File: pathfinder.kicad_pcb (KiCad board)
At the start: 2 copper layers, 59 x 46 mm, 12 parts, among them SW1 SW_Push, SW2 SW_Push, SW3 SW_Push, U1 XIAO-RP2040-DIP

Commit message: doing silkboard designs
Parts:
- moved D2 0.38 mm to (129.5, 112.2)
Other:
- board text added: "Keystorm X3"

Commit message: more silkscreen designs cuz why not
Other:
- board text added: "@hackclub"
- board text added: "made by: https://shashwat.cc"
- board text added: "oss hw"

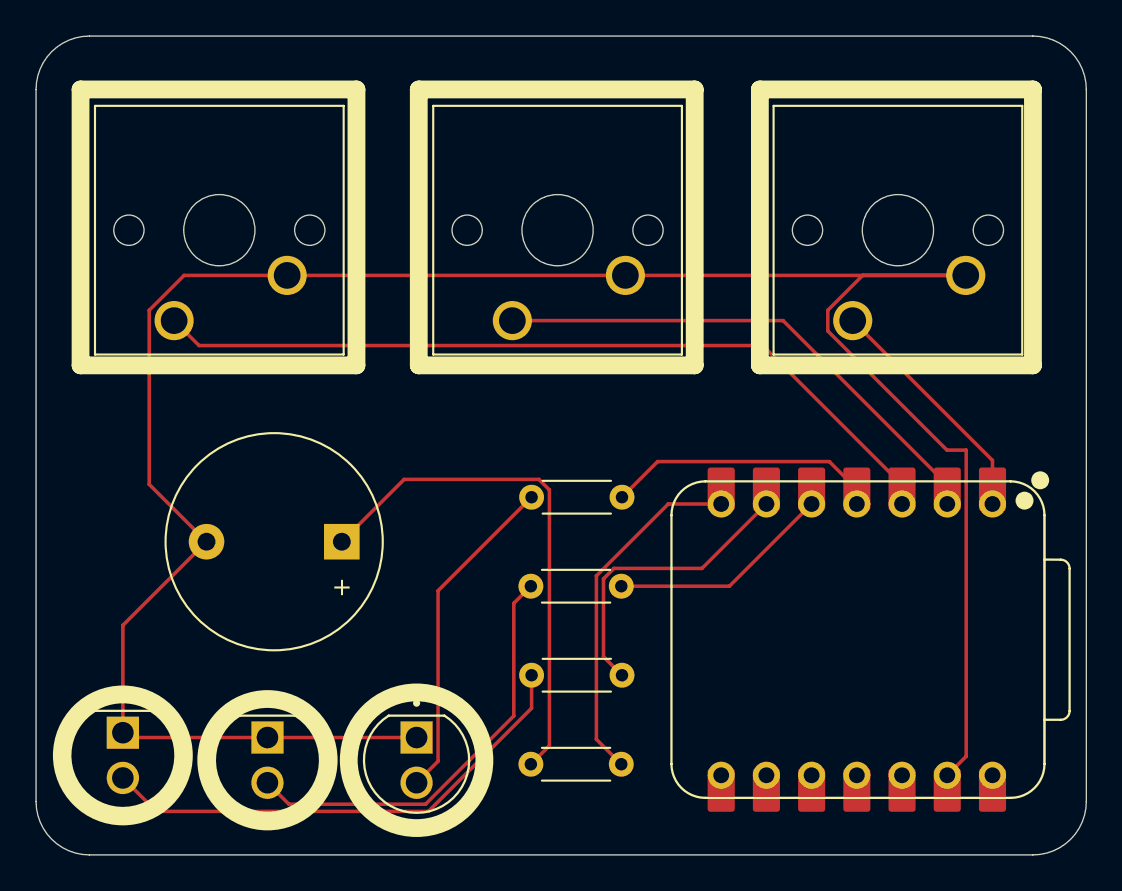
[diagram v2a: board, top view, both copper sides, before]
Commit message: added a BOM, done some final changes & added a README file
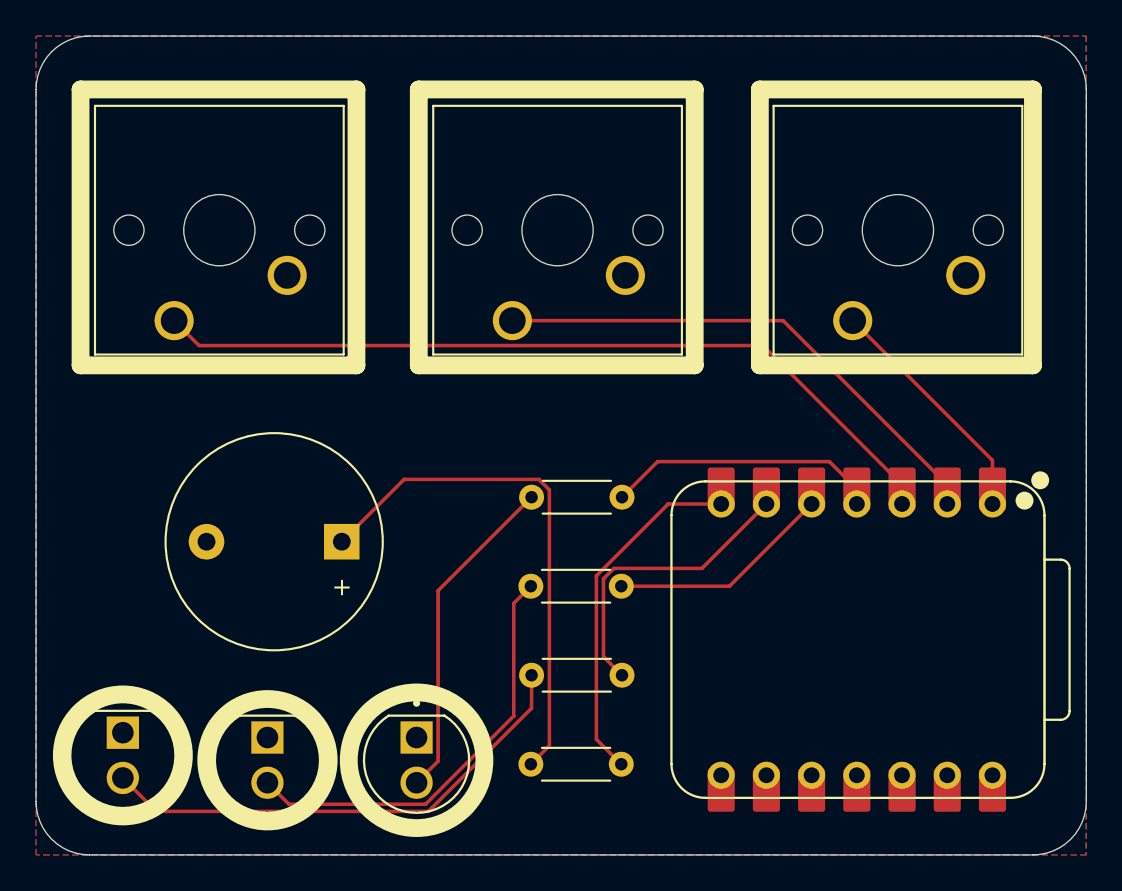
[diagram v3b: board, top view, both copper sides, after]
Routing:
- net GND: track 129.7 -> 0.76 mm
- added copper zone on B.Cu, net GND
- added copper zone on F.Cu, net GND
